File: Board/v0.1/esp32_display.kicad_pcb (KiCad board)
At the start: 2 copper layers, 90.5 x 69 mm, 59 parts, among them J1 Conn_01x06_Male, J2 USB_B_Micro, SW1 RST_BTN, SW2 SCREEN_OFF_BTN, U1 ESP32-WROOM-32, U2 MAX1821, U3 Display_ILI9341

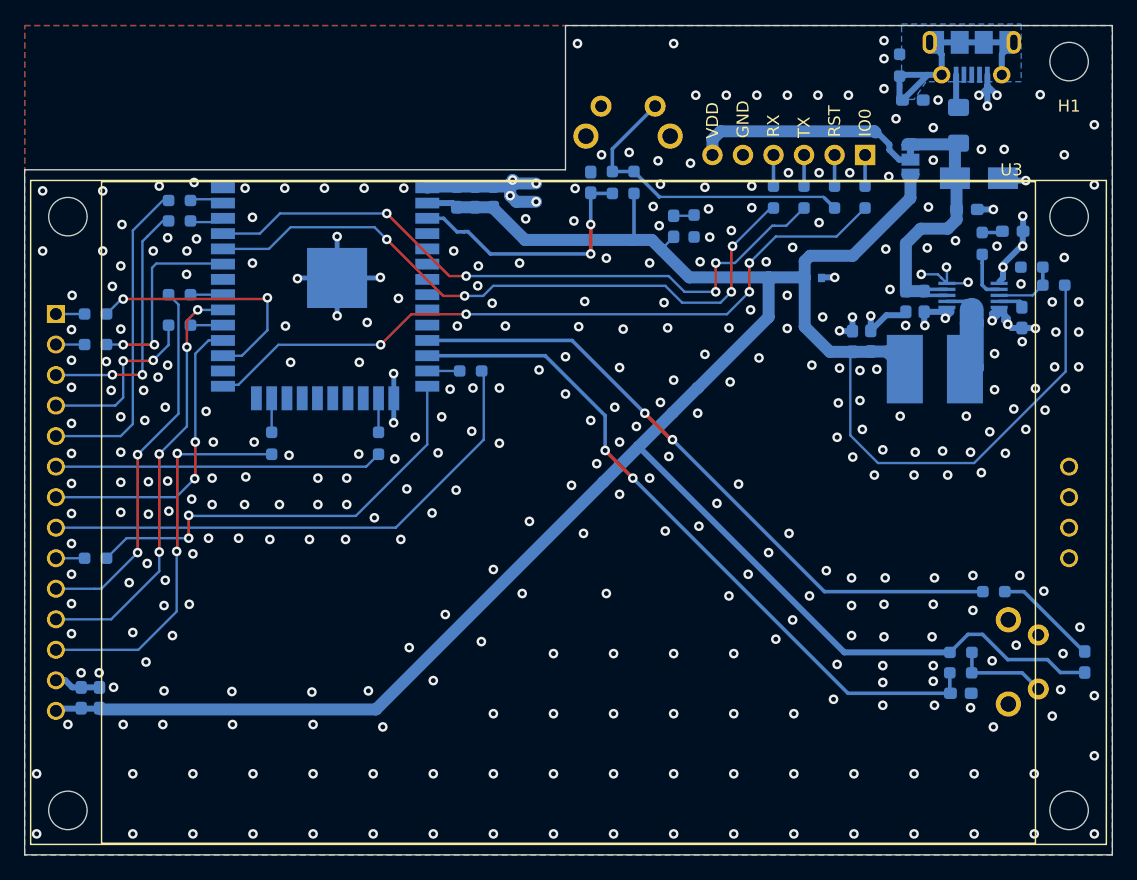
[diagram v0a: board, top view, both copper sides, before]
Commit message: Fix ILI9341 display symbol (pin numbering)
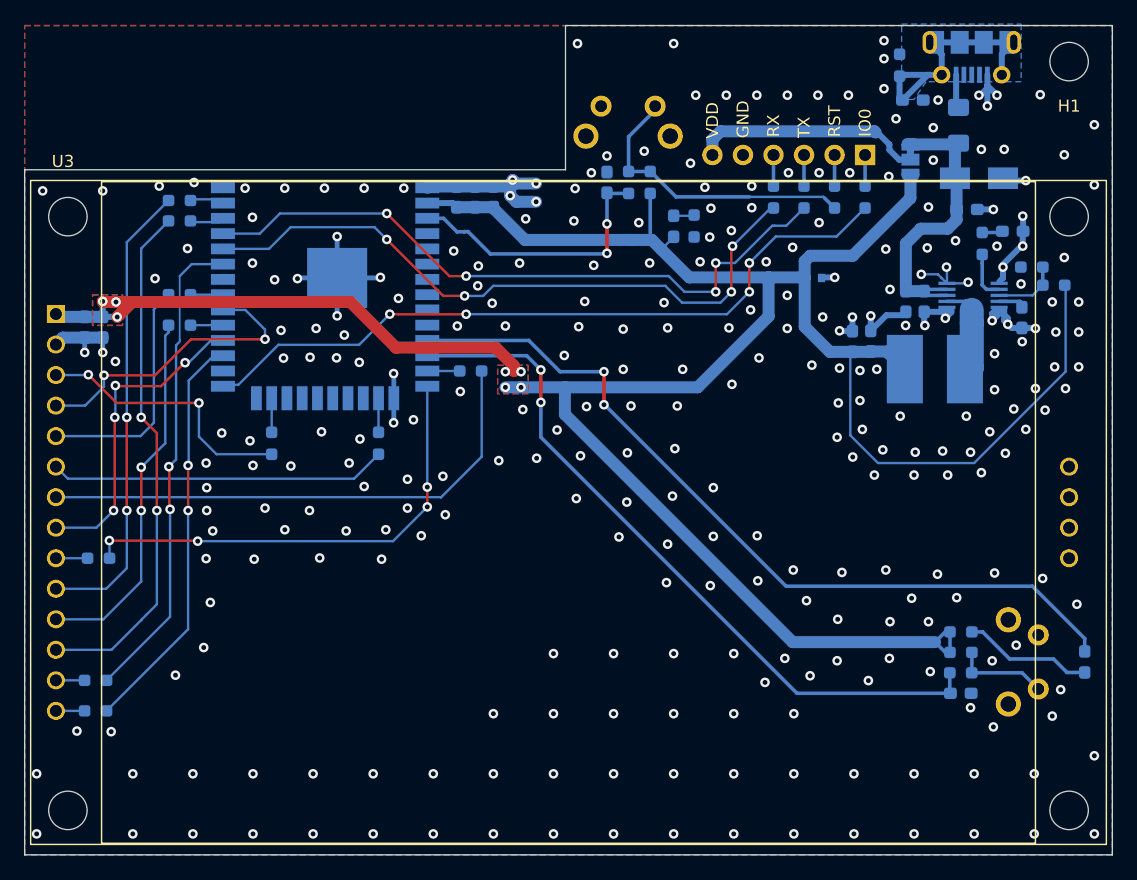
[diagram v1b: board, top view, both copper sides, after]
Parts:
- removed REF**: FCC-Logo_7.3x6mm_SilkScreen, Symbol:FCC-Logo_7.3x6mm_SilkScreen
- removed REF**: OSHW-Logo_7.5x8mm_SilkScreen, Symbol:OSHW-Logo_7.5x8mm_SilkScreen
- removed REF**: CE-Logo_8.5x6mm_SilkScreen, Symbol:CE-Logo_8.5x6mm_SilkScreen
- moved R21 33.0 mm to (92.9, 89.0)
- moved C13 30.8 mm to (92.0, 57.1), turned to -90 degrees
- moved C12 30.8 mm to (93.5, 57.1), turned to -90 degrees
- moved R22 27.9 mm to (92.9, 86.5)
- moved R1 4.33 mm to (164.9, 82.5), turned to 0 degrees
- moved R4 1.35 mm to (139.1, 45.1)
- moved C5 1.35 mm to (135.4, 45.1)
- moved R5 1.35 mm to (137.2, 45.1)
- moved R23 0.25 mm to (93.2, 76.3), turned to 180 degrees
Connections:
- D1 pad 1: Net-(D1-Pad1) -> /MCU/LED_STATUS
- D1 pad 2: +3V3 -> Net-(R1-Pad2)
- R1 pad 1: Net-(D1-Pad1) -> +3V3
- R1 pad 2: /MCU/LED_STATUS -> Net-(R1-Pad2)
- R23 pad 1: Net-(R23-Pad1) -> /MCU/DISP.SPI_MISO
- R23 pad 2: /MCU/DISP.SPI_MISO -> Net-(R23-Pad2)
- U3 pad 1: Net-(R21-Pad1) -> +3V3
- U3 pad 10: /MCU/DISP.DC -> /MCU/TOUCH.SPI_CLK
- U3 pad 11: /MCU/DISP.RST -> /MCU/TOUCH.SPI_CS
- U3 pad 12: /MCU/DISP.SPI_CS -> /MCU/TOUCH.SPI_MOSI
- U3 pad 13: GND -> Net-(R22-Pad1)
- U3 pad 14: +3V3 -> Net-(R21-Pad1)
- U3 pad 2: Net-(R22-Pad1) -> GND
- U3 pad 3: /MCU/TOUCH.SPI_MOSI -> /MCU/DISP.SPI_CS
- U3 pad 4: /MCU/TOUCH.SPI_CS -> /MCU/DISP.RST
- U3 pad 5: /MCU/TOUCH.SPI_CLK -> /MCU/DISP.DC
- U3 pad 7: /MCU/DISP.BCKL -> /MCU/DISP.SPI_CLK
- U3 pad 8: /MCU/DISP.SPI_CLK -> /MCU/DISP.BCKL
- U3 pad 9: Net-(R23-Pad1) -> Net-(R23-Pad2)
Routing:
- net /MCU/TOUCH.SPI_MISO: track 16.5 -> 40.2 mm
- net /MCU/TOUCH.SPI_MOSI: track 20.7 -> 43.4 mm
- net /MCU/TOUCH.SPI_CS: track 15.0 -> 30.7 mm
- net /MCU/TOUCH.IRQ: track 21.2 -> 34.0 mm
- net /MCU/LED_STATUS: track 54.9 -> 67.7 mm
- net /MCU/TOUCH.SPI_CLK: track 26.5 -> 38.6 mm, vias 0 -> 2
- net /MCU/DISP.DC: track 31.4 -> 19.8 mm, vias 2 -> 0
- net Net-(R1-Pad2): track 0.00 -> 10.8 mm
- net /MCU/DISP.RST: track 35.5 -> 25.2 mm, vias 4 -> 2
- net /MCU/DISP.SPI_CS: track 32.5 -> 22.3 mm
- net Net-(D1-Pad1): track 8.71 -> 0.00 mm
- net +3V3: track 226.3 -> 222.5 mm, vias 0 -> 7
- net GND: track 74.1 -> 76.7 mm, vias 364 -> 292
- net Net-(R23-Pad2): track 0.00 -> 2.64 mm
- net /MCU/DISP.SPI_MISO: track 36.6 -> 39.2 mm, vias 2 -> 4
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- added copper zone on B.Cu, net +3V3
- added copper zone on F.Cu, net +3V3

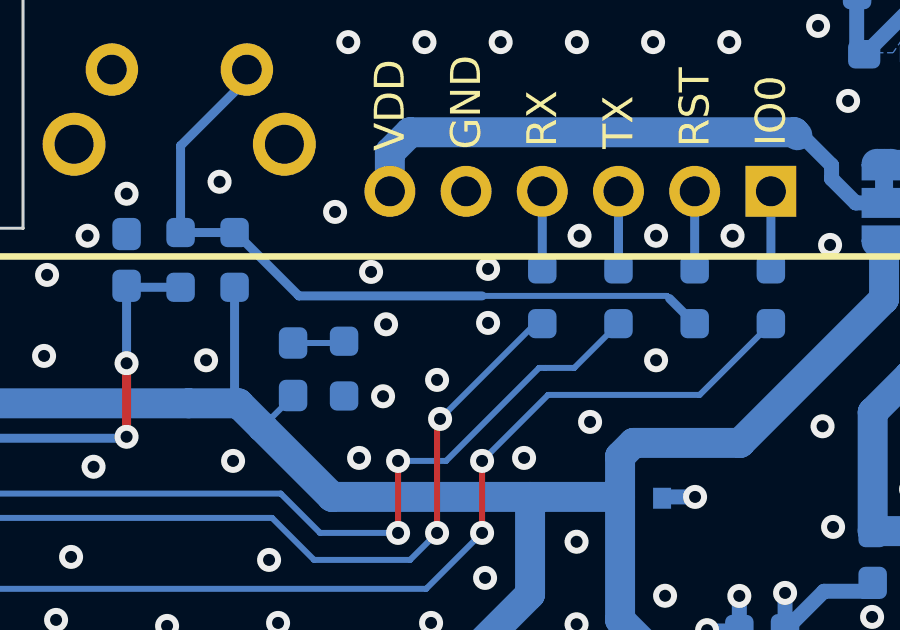
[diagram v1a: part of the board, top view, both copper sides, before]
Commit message: Add jumper for 3.3V power LED
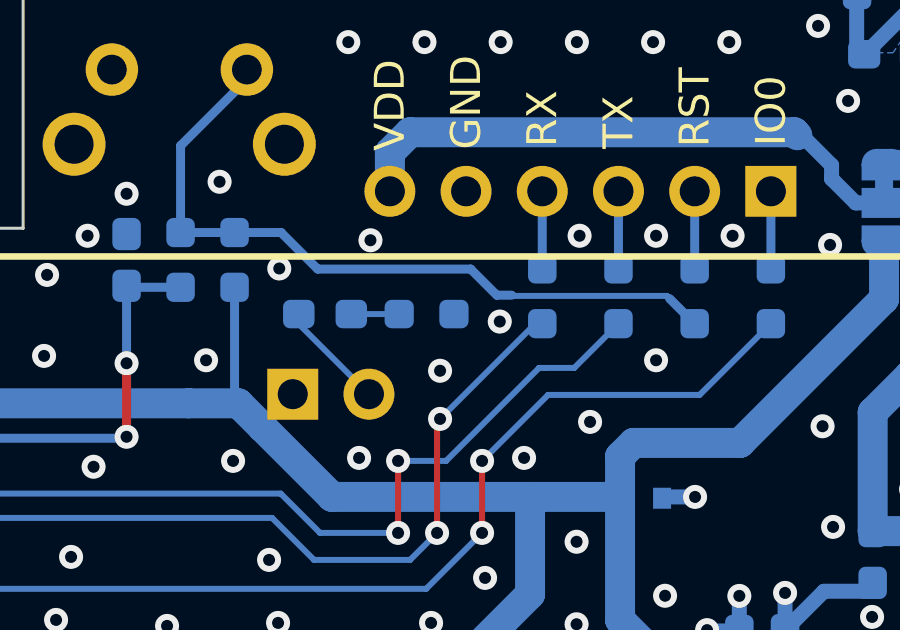
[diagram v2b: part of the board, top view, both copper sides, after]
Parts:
- added JP2: Jumper_2_Bridged, Connector_PinHeader_2.54mm:PinHeader_1x02_P2.54mm_Horizontal, B.Cu at (141.0, 49.5)
- moved R20 3.30 mm to (145.4, 46.9), turned to 0 degrees
- moved D3 2.13 mm to (142.1, 46.9), turned to 180 degrees
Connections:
- D3 pad 2: +3V3 -> Net-(D3-Pad2)
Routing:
- net Net-(D3-Pad2): track 0.00 -> 3.64 mm
- net GND: vias 292 -> 289
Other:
- board text added: "PWR LED"
- board text removed: "3.3V PWR"

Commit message: Add labels to unused pins
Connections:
- U1 pad 10: unconnected-(U1-Pad10) -> /MCU/IO25
- U1 pad 24: unconnected-(U1-Pad24) -> /MCU/IO2
- U1 pad 26: unconnected-(U1-Pad26) -> /MCU/IO4
- U1 pad 6: unconnected-(U1-Pad6) -> /MCU/IO34
- U1 pad 7: unconnected-(U1-Pad7) -> /MCU/IO35
- U1 pad 8: unconnected-(U1-Pad8) -> /MCU/IO32
- U1 pad 9: unconnected-(U1-Pad9) -> /MCU/IO33
